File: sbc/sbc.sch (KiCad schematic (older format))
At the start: 19 parts, among them J1 USB_B_Micro, J2 PB, J3 PA, SW1 RESET, U1 DS1813, U2 WD65C02, U3 28C256, U4 HM62256BLP, U5 WD65C22, U6 7400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

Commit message: SBC: Fix v1.0 errata
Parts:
- removed SW1: RESET, switch:SW_TH_Tactile_Omron_B3F-10xx, symbol switch:SW_Push_Dual
- removed X1: CXO_DIP14, oscillator:Oscillator_DIP-14, symbol oscillator:CXO_DIP14
- added SW1: RESET, switch:SW_TH_Tactile_Omron_B3F-10xx, symbol switch_tactile:SW_Tactile_Push
- added X1: 2Mhz, oscillator:Oscillator_DIP-8, symbol oscillator:CXO_DIP8
- C1: value 100uf -> 220uf; footprint capacitor:CP_Radial_D5.0mm_P2.50mm -> capacitor:CP_Radial_D8.0mm_P2.50mm
- U4: value HM62256BLP -> 62256
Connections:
- net +5V: now also X1.8 (Vcc)
- net GND: now also C1.2, J1.5 (GND), SW1.3, X1.4 (GND)
- net at U2.37 (PHI2), U5.25 (PHI2), U6.1: now also X1.5 (OUT)
- net at J2.12 (Pin_12), J3.12 (Pin_12), U1.1 (/RST)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: now also SW1.1
- no-connect marks 14 -> 12
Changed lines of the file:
@@
 Sheet 1 1
 Title "6502 SBC"
-Date "2021-09-09"
-Rev "1.0"
+Date "2021-10-02"
+Rev "1.1"
 Comp ""
 Comment1 ""
@@
 P 6500 3200
 F 0 "U4" H 6500 4281 50  0000 C CNN
-F 1 "HM62256BLP" H 6500 4190 50  0000 C CNN
+F 1 "62256" H 6500 4190 50  0000 C CNN
 F 2 "dip:DIP-28_W15.24mm_Socket" H 6500 3100 50  0001 C CNN
 F 3 "https://web.mit.edu/6.115/www/document/62256.pdf" H 6500 3100 50  0001 C CNN
@@
 Entry Wire Line
 	8400 3000 8300 2900
-$Comp
-L 65xx:WD65C22 U5
-U 1 1 6104D277
-P 9200 3500
-F 0 "U5" V 9253 2422 60  0000 R CNN
-F 1 "WD65C22" V 9147 2422 60  0000 R CNN
-F 2 "dip:DIP-40_W15.24mm_Socket" H 8700 3700 60  0001 C CNN
-F 3 "" H 8700 3700 60  0000 C CNN
-	1    9200 3500
-	-1   0    0    1
-$EndComp
 Wire Wire Line
 	8550 2800 8050 2800
@@
 	7650 2850 7650 4850
 $Comp
-L oscillator:CXO_DIP14 X1
-U 1 1 61142AF5
-P 8400 5550
-F 0 "X1" H 8744 5596 50  0000 L CNN
-F 1 "CXO_DIP14" H 8744 5505 50  0000 L CNN
-F 2 "oscillator:Oscillator_DIP-14" H 8850 5200 50  0001 C CNN
-F 3 "http://cdn-reichelt.de/documents/datenblatt/B400/OSZI.pdf" H 8300 5550 50  0001 C CNN
-	1    8400 5550
-	1    0    0    -1
-$EndComp
-$Comp
 L power:GND #PWR024
 U 1 1 6117B29B
@@
 L power:GND #PWR09
 U 1 1 611C40F8
-P 2450 1550
-F 0 "#PWR09" H 2450 1300 50  0001 C CNN
-F 1 "GND" H 2455 1377 50  0000 C CNN
-F 2 "" H 2450 1550 50  0001 C CNN
-F 3 "" H 2450 1550 50  0001 C CNN
-	1    2450 1550
+P 2450 1500
+F 0 "#PWR09" H 2450 1250 50  0001 C CNN
+F 1 "GND" H 2455 1327 50  0000 C CNN
+F 2 "" H 2450 1500 50  0001 C CNN
+F 3 "" H 2450 1500 50  0001 C CNN
+	1    2450 1500
 	1    0    0    -1
 $EndComp
@@
 	3150 1100 3150 1700
 Connection ~ 3150 1700
-$Comp
-L switch:SW_Push_Dual SW1
-U 1 1 611DA4FE
-P 2750 1350
-F 0 "SW1" V 2704 1498 50  0000 L CNN
-F 1 "RESET" V 2795 1498 50  0000 L CNN
-F 2 "switch:SW_TH_Tactile_Omron_B3F-10xx" H 2750 1550 50  0001 C CNN
-F 3 "~" H 2750 1550 50  0001 C CNN
-	1    2750 1350
-	0    1    1    0
-$EndComp
-Wire Wire Line
-	2450 1550 2550 1550
-Wire Wire Line
-	2450 1300 2450 1550
-Connection ~ 2450 1550
-NoConn ~ 2750 1150
-NoConn ~ 2750 1550
-Wire Wire Line
-	2450 1100 2550 1100
-Wire Wire Line
-	2550 1150 2550 1100
-Connection ~ 2550 1100
-Wire Wire Line
-	2550 1100 3150 1100
+Wire Wire Line
+	2450 1300 2450 1500
 NoConn ~ 850  1500
 NoConn ~ 1250 1100
@@
 P 1450 1050
 F 0 "C1" H 1565 1096 50  0000 L CNN
-F 1 "100uf" H 1565 1005 50  0000 L CNN
-F 2 "capacitor:CP_Radial_D5.0mm_P2.50mm" H 1450 1050 50  0001 C CNN
+F 1 "220uf" H 1565 1005 50  0000 L CNN
+F 2 "capacitor:CP_Radial_D8.0mm_P2.50mm" H 1450 1050 50  0001 C CNN
 F 3 "~" H 1450 1050 50  0001 C CNN
 	1    1450 1050
@@
 Wire Wire Line
 	1450 1200 1450 1500
-Wire Wire Line
-	1450 1500 950  1500
 $Comp
 L power:+5V #PWR0101
@@
 $EndComp
 Connection ~ 1450 900
+Wire Wire Line
+	2450 1100 2550 1100
+$Comp
+L switch_tactile:SW_Tactile_Push SW1
+U 1 1 615C92B6
+P 2550 1300
+F 0 "SW1" V 2504 1448 50  0000 L CNN
+F 1 "RESET" V 2595 1448 50  0000 L CNN
+F 2 "switch:SW_TH_Tactile_Omron_B3F-10xx" H 2550 1500 50  0001 C CNN
+F 3 "~" H 2550 1500 50  0001 C CNN
+	1    2550 1300
+	0    1    1    0
+$EndComp
+Connection ~ 2550 1100
+Wire Wire Line
+	2550 1100 3150 1100
+Wire Wire Line
+	2550 1500 2450 1500
+$Comp
+L power:GND #PWR0102
+U 1 1 61630166
+P 1450 1500
+F 0 "#PWR0102" H 1450 1250 50  0001 C CNN
+F 1 "GND" H 1455 1327 50  0000 C CNN
+F 2 "" H 1450 1500 50  0001 C CNN
+F 3 "" H 1450 1500 50  0001 C CNN
+	1    1450 1500
+	1    0    0    -1
+$EndComp
+Connection ~ 2450 1500
+$Comp
+L 65xx:WD65C22 U5
+U 1 1 6104D277
+P 9200 3500
+F 0 "U5" H 9200 2250 60  0000 C CNN
+F 1 "WD65C22" H 9200 2350 60  0000 C CNN
+F 2 "dip:DIP-40_W15.24mm_Socket" H 8700 3700 60  0001 C CNN
+F 3 "" H 8700 3700 60  0000 C CNN
+	1    9200 3500
+	-1   0    0    1
+$EndComp
+Wire Wire Line
+	950  1500 1450 1500
+$Comp
+L oscillator:CXO_DIP8 X1
+U 1 1 6176538C
+P 8400 5550
+F 0 "X1" H 8744 5596 50  0000 L CNN
+F 1 "2Mhz" H 8744 5505 50  0000 L CNN
+F 2 "oscillator:Oscillator_DIP-8" H 8850 5200 50  0001 C CNN
+F 3 "http://cdn-reichelt.de/documents/datenblatt/B400/OSZI.pdf" H 8300 5550 50  0001 C CNN
+	1    8400 5550
+	1    0    0    -1
+$EndComp
+Connection ~ 1450 1500
 $Comp
 L connector:USB_B_Micro J1
-U 1 1 61270BB5
+U 1 1 6172B07E
 P 950 1100
 F 0 "J1" H 1007 1567 50  0000 C CNN

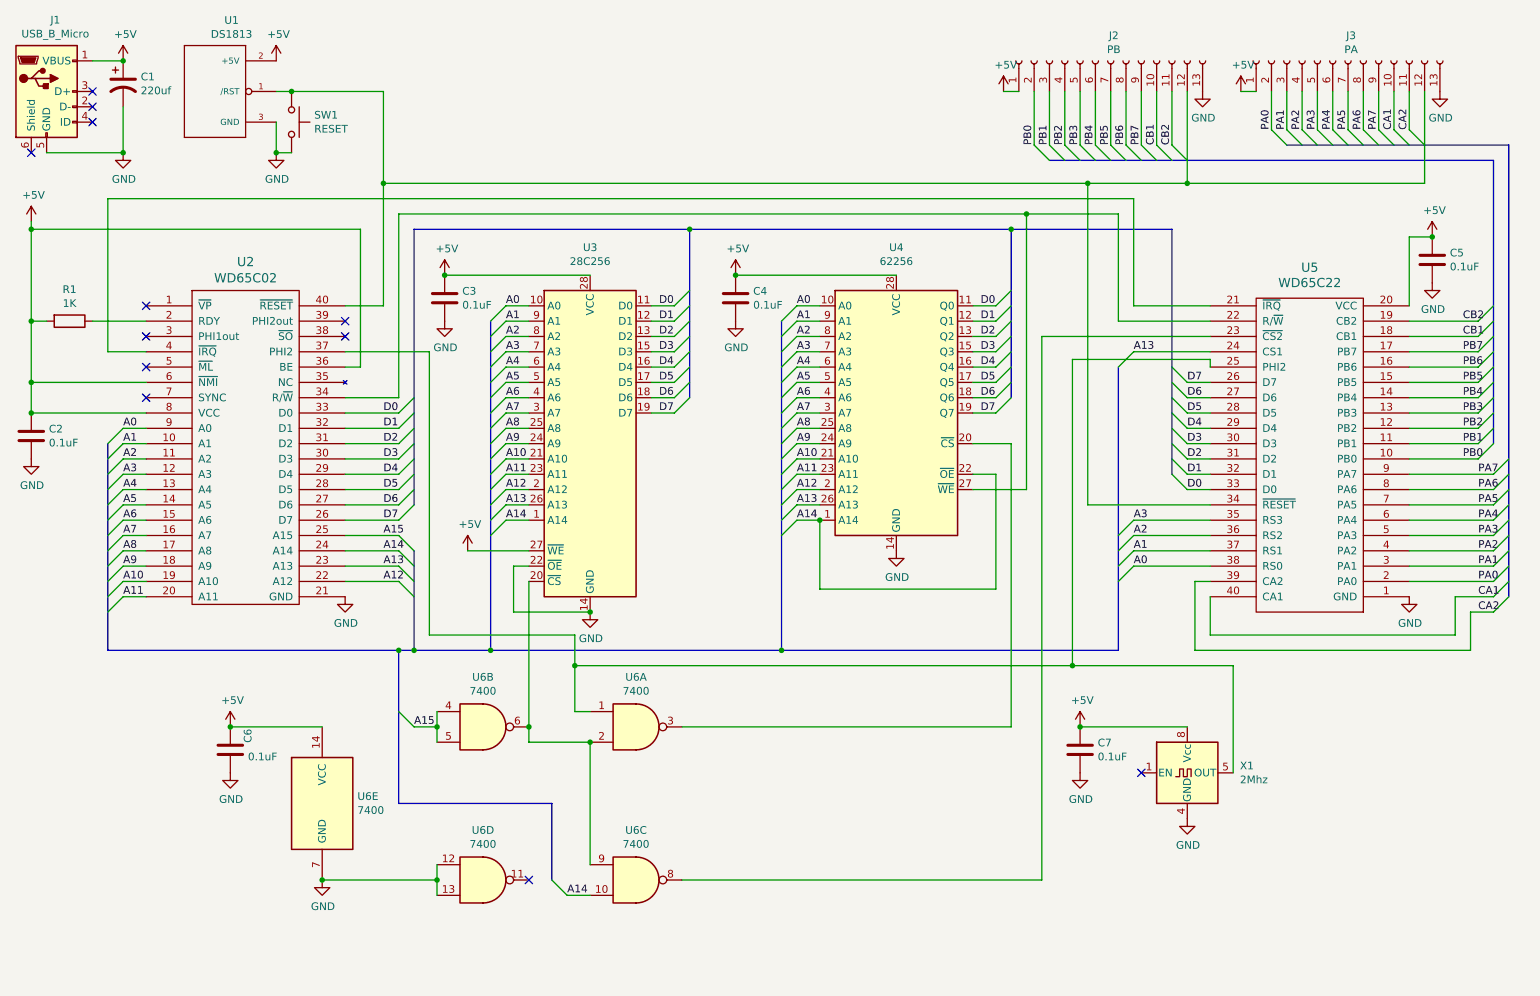
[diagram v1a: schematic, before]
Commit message: SBC v2.0
Changes:

 - Second VIA
 - NMI button (hardware debounced)
 - 5 status LEDs (power and each VIA port)
 - Ground and power planes
 - Smaller footprint RAM and oscillator
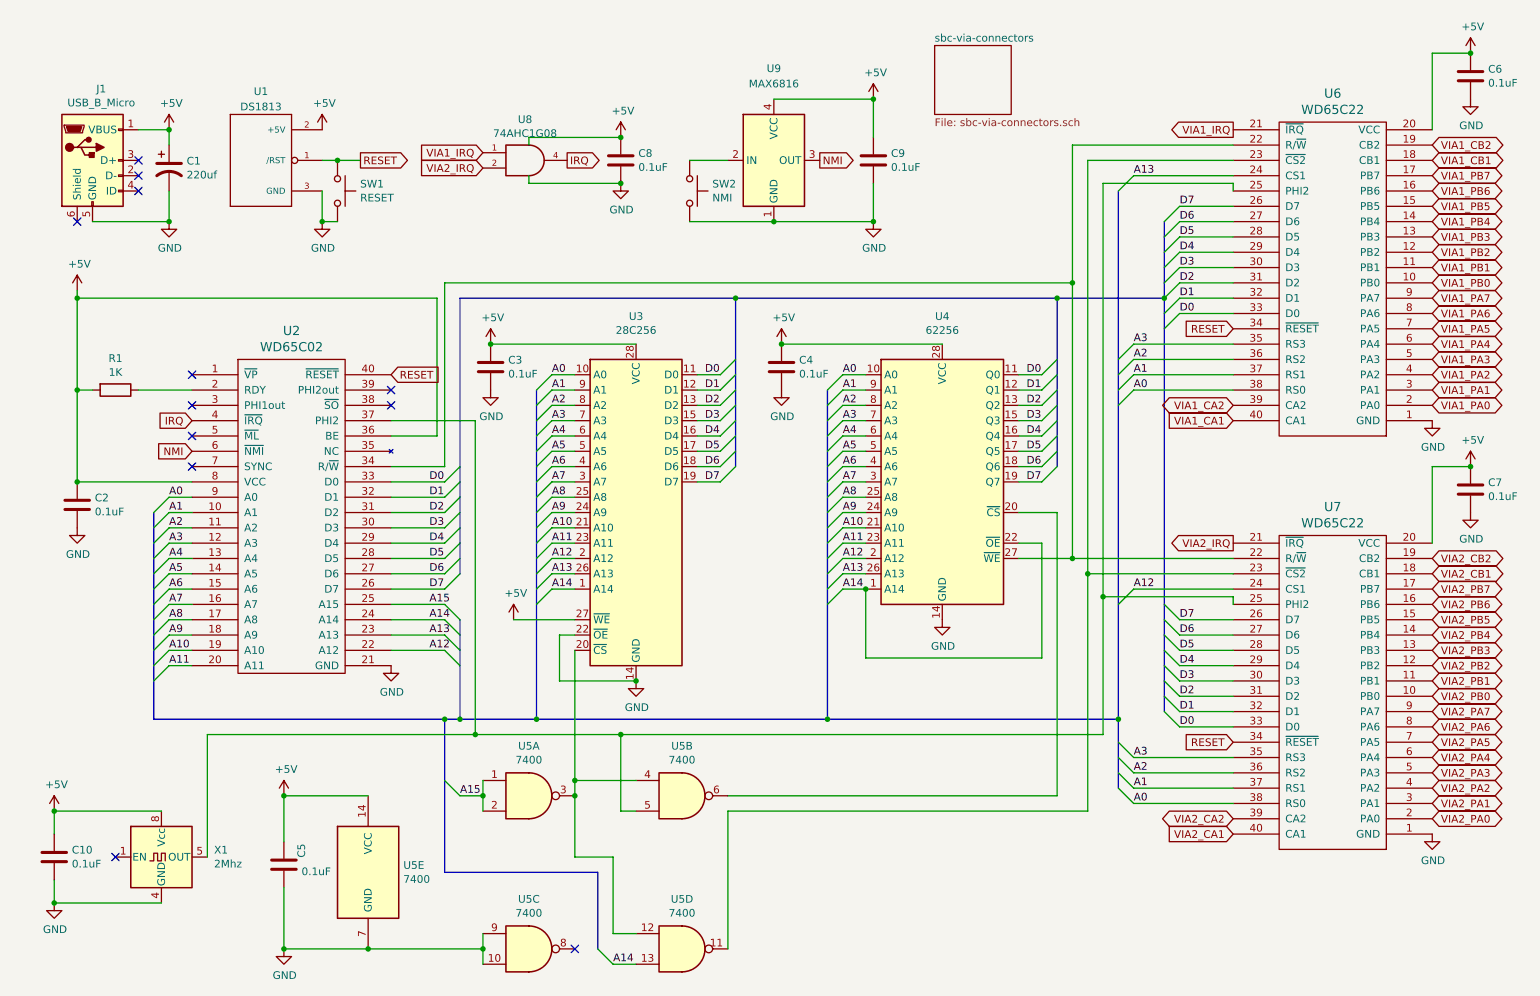
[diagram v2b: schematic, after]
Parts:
- removed J2: PB, connector:PinSocket_1x13_P2.54mm_Vertical, symbol connector:Conn_01x13_Female
- removed J3: PA, connector:PinSocket_1x13_P2.54mm_Vertical, symbol connector:Conn_01x13_Female
- removed U5: WD65C22, dip:DIP-40_W15.24mm_Socket, symbol 65xx:WD65C22
- added C7, C8, C9: 0.1uF, capacitor:C_Rect_L4.0mm_W2.5mm_P2.50mm, symbol device:C
- added SW2: NMI, switch:SW_TH_Tactile_Omron_B3F-10xx, symbol switch_tactile:SW_Tactile_Push
- added U6, U7: WD65C22, dip:DIP-40_W15.24mm_Socket, symbol 65xx:WD65C22
- added U8: 74AHC1G08, to_sot_smd:SOT-23-5_HandSoldering, symbol 74xGxx:74AHC1G08
- added U9: MAX6816, to_sot_smd:SOT-143_Handsoldering, symbol interface:MAX6816
- C1: footprint capacitor:CP_Radial_D8.0mm_P2.50mm -> capacitor:CP_Radial_D6.3mm_P2.50mm
- C10: renamed from C7; footprint capacitor:C_Rect_L4.6mm_W3.0mm_P2.50mm_MKS02_FKP02 -> capacitor:C_Rect_L4.0mm_W2.5mm_P2.50mm
- C2, C3, C4: footprint capacitor:C_Rect_L4.6mm_W3.0mm_P2.50mm_MKS02_FKP02 -> capacitor:C_Rect_L4.0mm_W2.5mm_P2.50mm
- C5: renamed from C6; footprint capacitor:C_Rect_L4.6mm_W3.0mm_P2.50mm_MKS02_FKP02 -> capacitor:C_Rect_L4.0mm_W2.5mm_P2.50mm
- C6: renamed from C5; footprint capacitor:C_Rect_L4.6mm_W3.0mm_P2.50mm_MKS02_FKP02 -> capacitor:C_Rect_L4.0mm_W2.5mm_P2.50mm
- J1: footprint connector_usb:USB_Micro-B_Amphenol_10118194_Horizontal -> connector_usb_handsoldering:USB_Micro-B_Amphenol_10118194_Horizontal_HandSoldering
- U1: footprint to_sot:TO-92_Inline -> to_sot_smd:SOT-23_Handsoldering
- U4: footprint dip:DIP-28_W15.24mm_Socket -> dip:DIP-28_W7.62mm_Socket
- renumbered U6 to U5
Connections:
- net +5V: now also C7.1, C8.1, C9.1, U6.20 (VCC), U7.20 (VCC), U8.5 (VCC), U9.4 (VCC); no longer U2.6 (~NMI)
- net A0: now also U6.38 (RS0), U7.38 (RS0)
- net A1: now also U6.37 (RS1), U7.37 (RS1)
- net A12: now also U7.24 (CS1)
- net A13: now also U6.24 (CS1)
- net A14: now also U5.13; no longer U5.10
- net A15: now also U5.1, U5.2; no longer U5.4, U5.5
- net A2: now also U6.36 (RS2), U7.36 (RS2)
- net A3: now also U6.35 (RS3), U7.35 (RS3)
- net D0: now also U6.33 (D0), U7.33 (D0)
- net D1: now also U6.32 (D1), U7.32 (D1)
- net D2: now also U6.31 (D2), U7.31 (D2)
- net D3: now also U6.30 (D3), U7.30 (D3)
- net D4: now also U6.29 (D4), U7.29 (D4)
- net D5: now also U6.28 (D5), U7.28 (D5)
- net D6: now also U6.27 (D6), U7.27 (D6)
- net D7: now also U6.26 (D7), U7.26 (D7)
- net GND: now also U5.10, U5.9, C7.2, C8.2, C9.2, SW2.3, U6.1 (GND), U7.1 (GND), U8.3 (GND), U9.1 (GND); no longer U5.12, U5.13
- net at U2.34 (R/~W), U4.27 (~WE): now also U6.22 (R/~W), U7.22 (R/~W)
- net at U2.37 (PHI2), X1.5 (OUT): now also U5.5, U6.25 (PHI2), U7.25 (PHI2); no longer U5.1
- net IRQ: now reaches U2.4 (~IRQ)
- net IRQ: now also U8.4
- net RESET: now reaches SW1.1, U1.1 (/RST), U2.40 (~RESET)
- net RESET: now also U6.34 (~RESET), U7.34 (~RESET)
- net at U5.3: now also U3.20 (~CS), U5.12, U5.4; no longer U4.20 (~CS)
- net at U5.11: now also U6.23 (~CS2), U7.23 (~CS2)
- new net: U4.20 (~CS), U5.6
- new net: SW2.1, U9.2 (IN)
- new net NMI: U2.6 (~NMI), U9.3 (OUT)
- new net VIA1_CA1: U6.40 (CA1)
- new net VIA1_CA2: U6.39 (CA2)
- new net VIA1_CB1: U6.18 (CB1)
- new net VIA1_CB2: U6.19 (CB2)
- new net VIA1_IRQ: U6.21 (~IRQ), U8.1
- new net VIA1_PA0: U6.2 (PA0)
- new net VIA1_PA1: U6.3 (PA1)
- new net VIA1_PA2: U6.4 (PA2)
- new net VIA1_PA3: U6.5 (PA3)
- new net VIA1_PA4: U6.6 (PA4)
- new net VIA1_PA5: U6.7 (PA5)
- new net VIA1_PA6: U6.8 (PA6)
- new net VIA1_PA7: U6.9 (PA7)
- new net VIA1_PB0: U6.10 (PB0)
- new net VIA1_PB1: U6.11 (PB1)
- new net VIA1_PB2: U6.12 (PB2)
- new net VIA1_PB3: U6.13 (PB3)
- new net VIA1_PB4: U6.14 (PB4)
- new net VIA1_PB5: U6.15 (PB5)
- new net VIA1_PB6: U6.16 (PB6)
- new net VIA1_PB7: U6.17 (PB7)
- new net VIA2_CA1: U7.40 (CA1)
- new net VIA2_CA2: U7.39 (CA2)
- new net VIA2_CB1: U7.18 (CB1)
- new net VIA2_CB2: U7.19 (CB2)
- new net VIA2_IRQ: U7.21 (~IRQ), U8.2
- new net VIA2_PA0: U7.2 (PA0)
- new net VIA2_PA1: U7.3 (PA1)
- new net VIA2_PA2: U7.4 (PA2)
- new net VIA2_PA3: U7.5 (PA3)
- new net VIA2_PA4: U7.6 (PA4)
- new net VIA2_PA5: U7.7 (PA5)
- new net VIA2_PA6: U7.8 (PA6)
- new net VIA2_PA7: U7.9 (PA7)
- new net VIA2_PB0: U7.10 (PB0)
- new net VIA2_PB1: U7.11 (PB1)
- new net VIA2_PB2: U7.12 (PB2)
- new net VIA2_PB3: U7.13 (PB3)
- new net VIA2_PB4: U7.14 (PB4)
- new net VIA2_PB5: U7.15 (PB5)
- new net VIA2_PB6: U7.16 (PB6)
- new net VIA2_PB7: U7.17 (PB7)
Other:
- moved on the sheet: C1, C10, C2, C3, C4, C5, C6, J1, R1, SW1, U1, U2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
